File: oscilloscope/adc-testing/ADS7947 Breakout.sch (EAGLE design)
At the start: 23 parts, among them U1 ADS7947SRTET

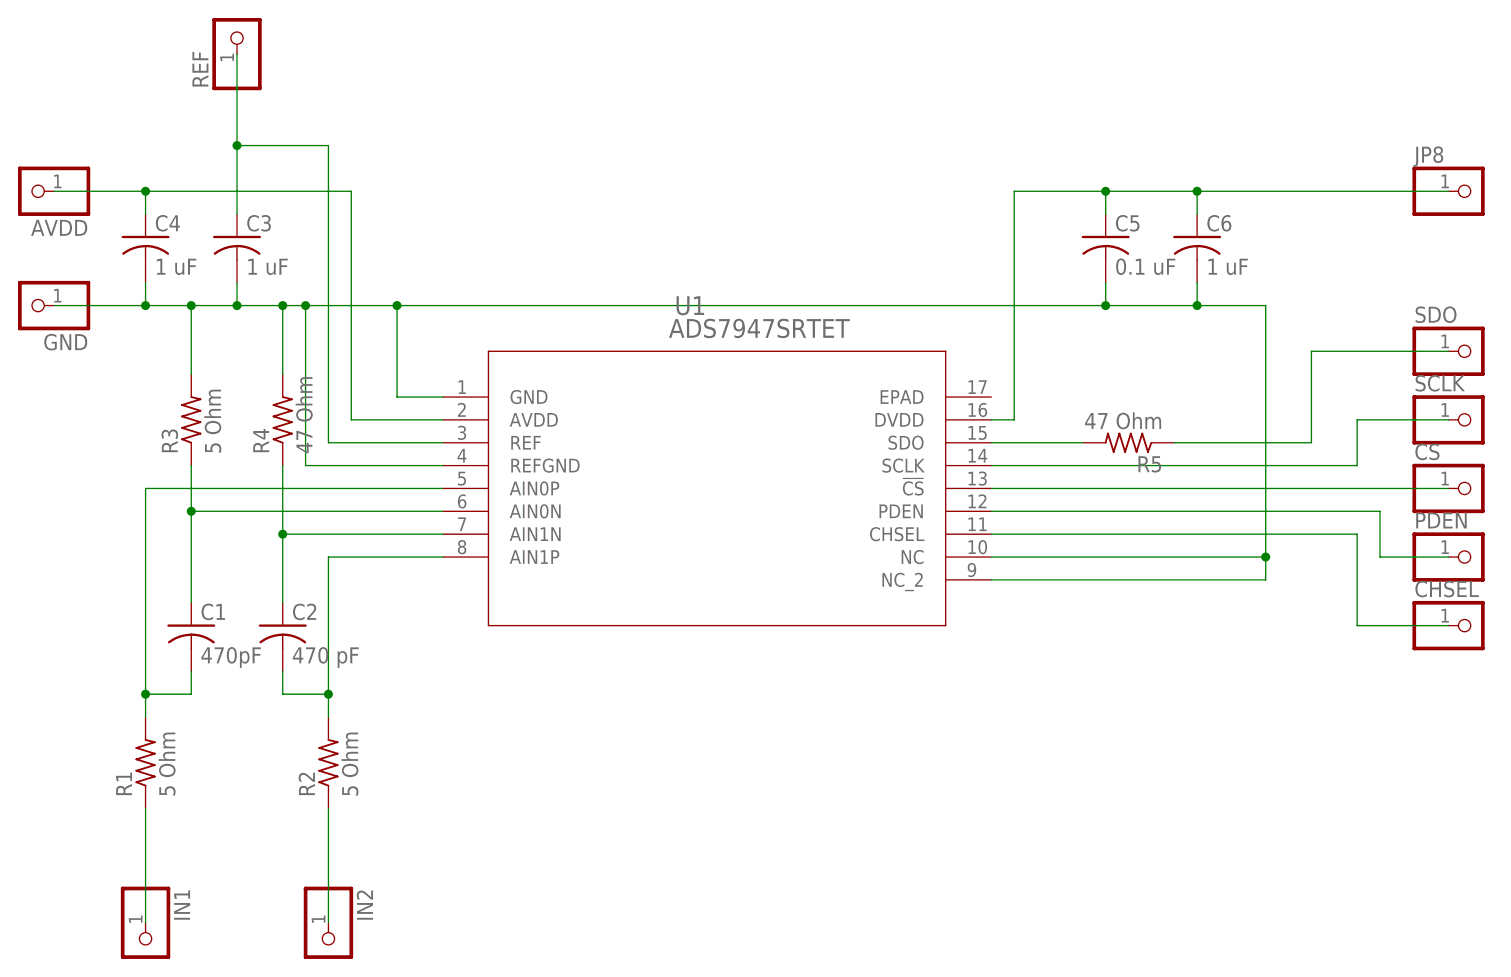
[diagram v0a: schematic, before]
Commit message: Fixed schematic, added NC pins
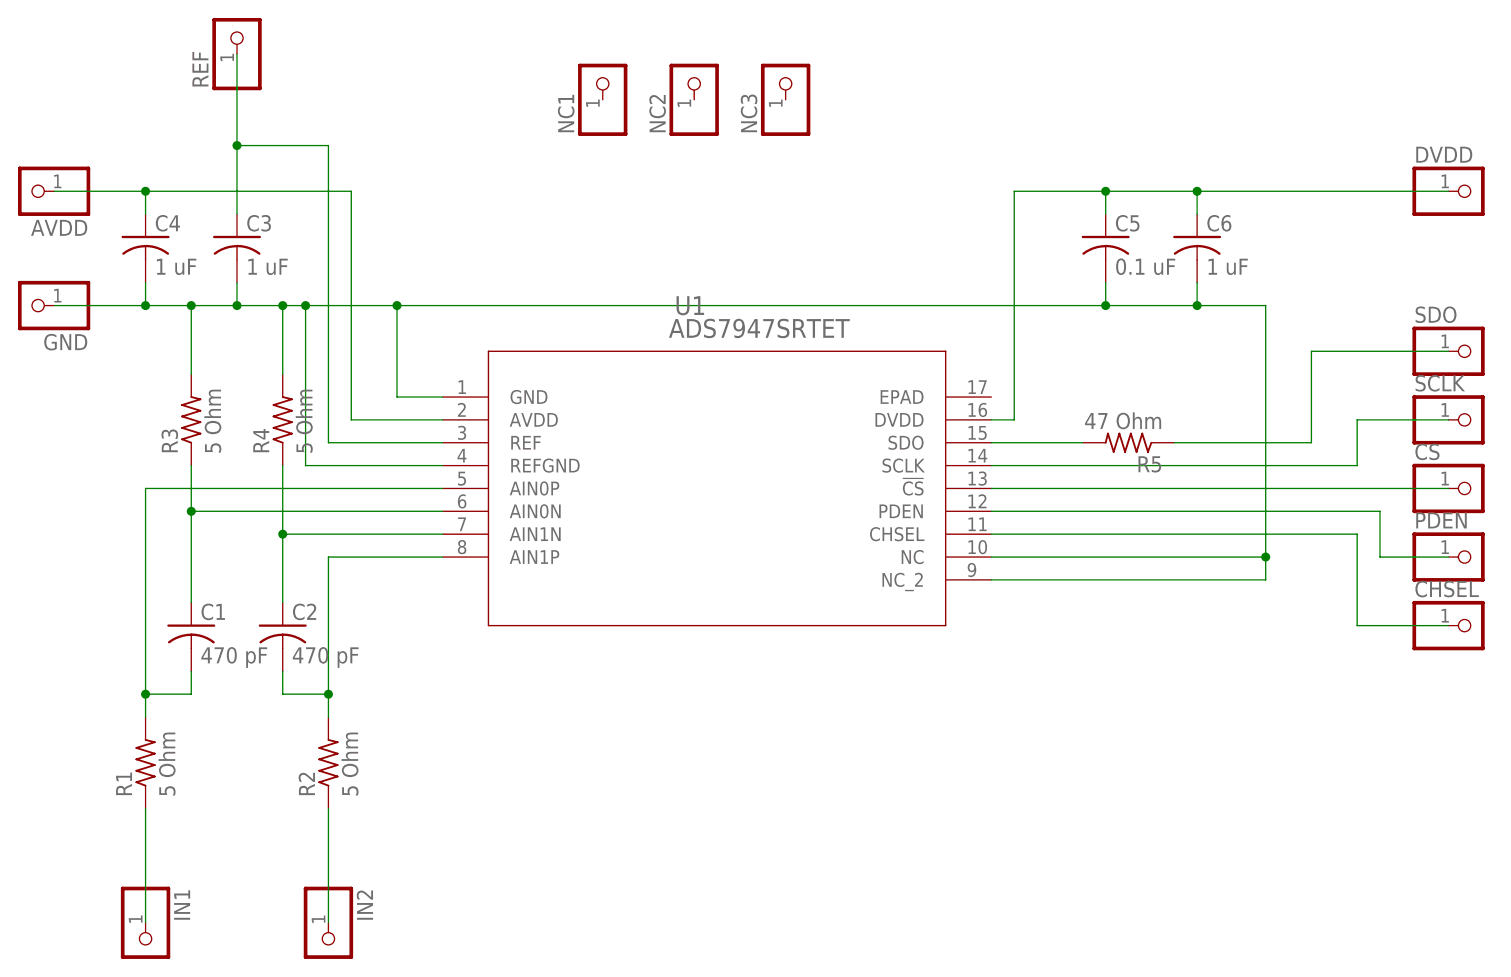
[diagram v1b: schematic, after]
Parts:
- added NC1, NC2, NC3: (no value), pinhead:PINHD-1X1
- C1: value 470pF -> 470 pF; device rcl:C-USC1206 -> rcl:C-USC0805
- C2, C3, C4, C5, C6: device rcl:C-USC1206 -> rcl:C-USC0805
- R1, R2, R3, R5: device rcl:R-US_R1206 -> rcl:R-US_R0805
- R4: value 47 Ohm -> 5 Ohm; device rcl:R-US_R1206 -> rcl:R-US_R0805
- renumbered JP8 to DVDD
